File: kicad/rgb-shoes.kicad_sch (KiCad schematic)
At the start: 14 parts, among them U1 L7805, U2 LM358, U3 Pico

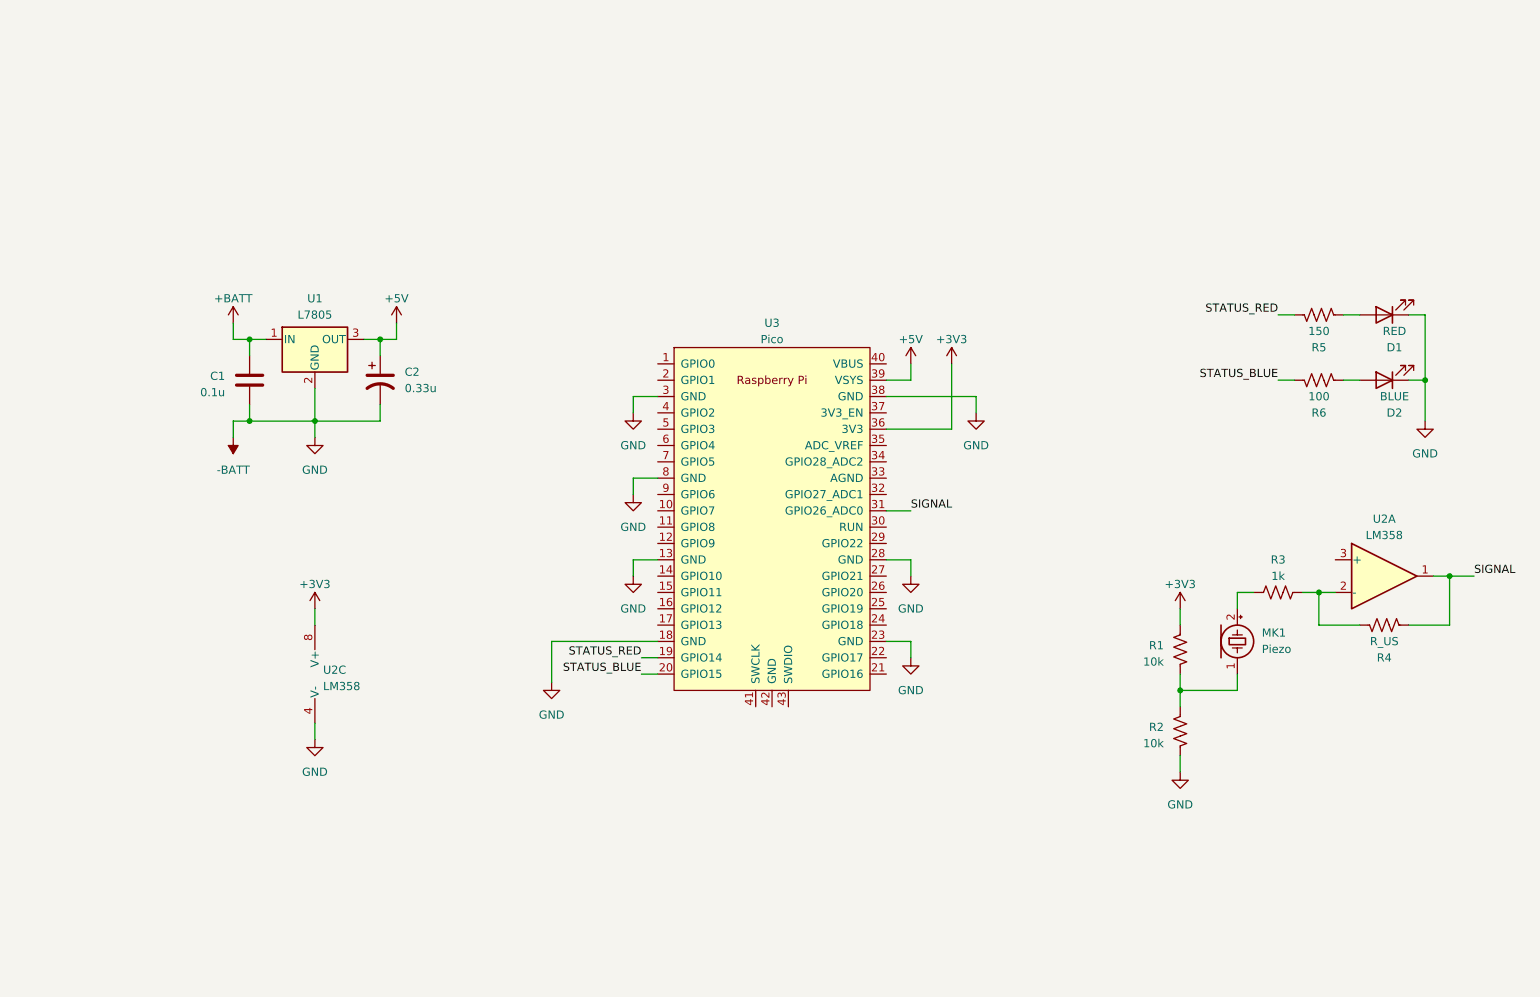
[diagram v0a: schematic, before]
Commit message: Updated schematic to include all components
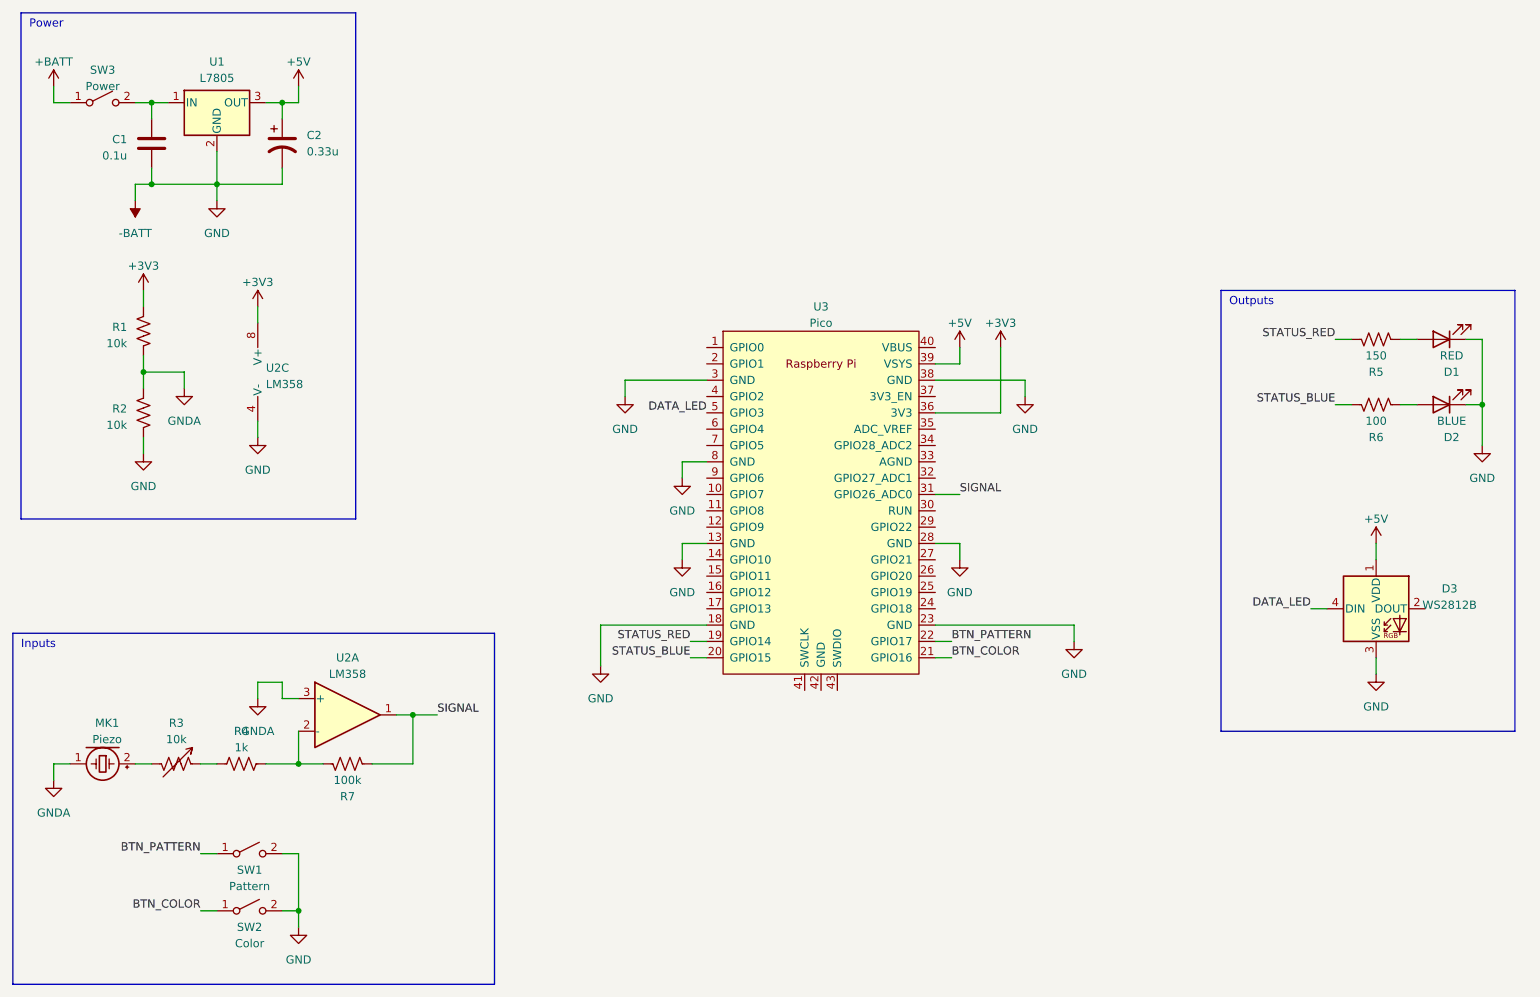
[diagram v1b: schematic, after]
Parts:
- removed R3: 1k, symbol Device:R_US
- added D3: WS2812B, LED_SMD:LED_WS2812B_PLCC4_5.0x5.0mm_P3.2mm, symbol LED:WS2812B
- added R3: 10k, symbol Device:R_Variable_US
- added R7: 100k, symbol Device:R_US
- added SW1: Pattern, symbol Switch:SW_SPST
- added SW2: Color, symbol Switch:SW_SPST
- added SW3: Power, symbol Switch:SW_SPST
- R4: value R_US -> 1k
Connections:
- net +5V: now also D3.1 (VDD)
- net +BATT: now also SW3.1 (A); no longer C1.1, U1.1 (IN)
- net -BATT: now also D3.3 (VSS), SW1.2 (B), SW2.2 (B)
- net SIGNAL: now also R7.1; no longer R4.1
- net BTN_COLOR: now reaches U3.21 (GPIO16)
- net BTN_COLOR: now also SW2.1 (A)
- net BTN_PATTERN: now reaches U3.22 (GPIO17)
- net BTN_PATTERN: now also SW1.1 (A)
- net DATA_LED: now reaches U3.5 (GPIO3)
- net DATA_LED: now also D3.4 (DIN)
- net at MK1.2 (+): now also R3.2
- net at R4.2, U2.2 (-): now also R7.2
- net GNDA: now reaches MK1.1 (-), R1.2, R2.1
- net GNDA: now also U2.3 (+)
- new net: C1.1, SW3.2 (B), U1.1 (IN)
- new net: R3.1, R4.1
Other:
- note added: "Inputs"
- note added: "Outputs"
- note added: "Power"
- moved on the sheet: C1, C2, D1, D2, R5, R6, U1, U2C, U3
